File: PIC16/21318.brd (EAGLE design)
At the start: 71.1 x 30.5 mm, 11 parts, among them U2 I50115

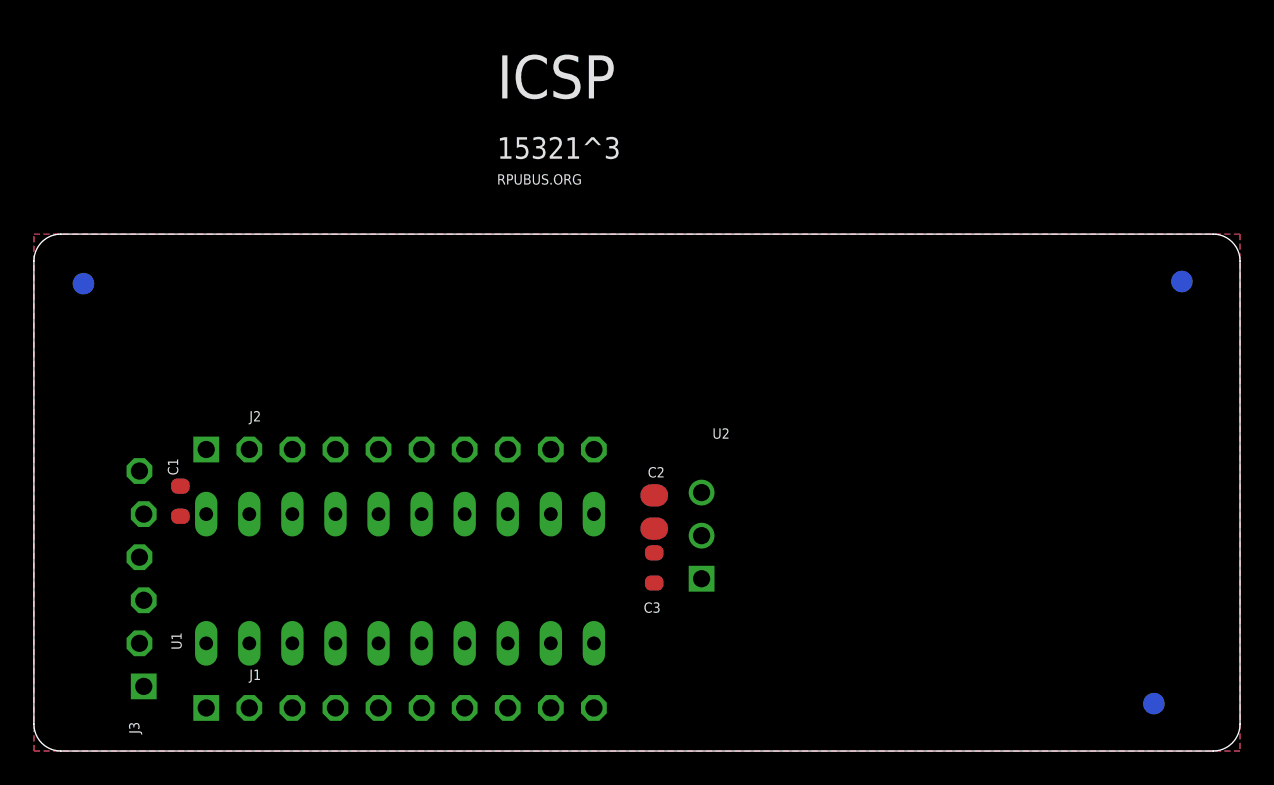
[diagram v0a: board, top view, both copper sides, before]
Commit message: PIC16
8pin, 14pin, and 20pin will work, just keep pin 1 fixed.
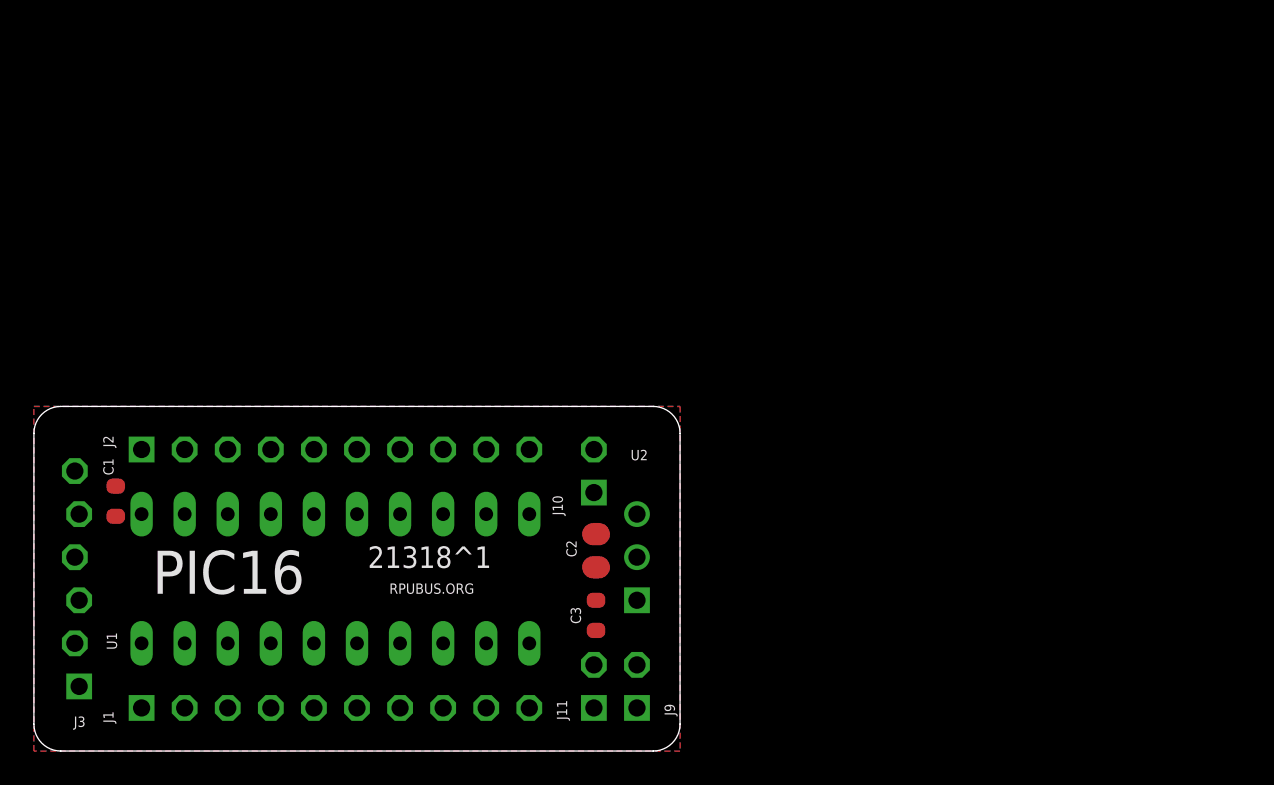
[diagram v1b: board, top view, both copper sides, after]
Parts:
- removed U$2, U$3, U$4: FIDUCIAL1.27, H-Fiducial:FIDUCIAL-1.27
- added J10, J11, J9: (no value), J-HDR2.54mm:1X2
- moved C3 4.42 mm to (33.1, 8.00), turned to 270 degrees
- moved C2 4.12 mm to (33.1, 11.8)
- moved U2 4.02 mm to (35.6, 8.89)
- moved J1 3.81 mm to (6.35, 2.54)
- moved J2 3.81 mm to (6.35, 17.8)
- moved C1 3.81 mm to (4.83, 14.7)
- moved J3 3.81 mm to (2.54, 3.81)
- moved U1 3.81 mm to (17.8, 10.2)
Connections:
- removed net N$1: J3.1, U1.4
- new net RA2: J2.4, U1.17
- new net RA3: J1.4, J3.1, U1.4
- new net RA4: J1.3, U1.3
- new net RA5: J1.2, U1.2
- new net RB4: J2.8, U1.13
- new net RB5: J2.9, U1.12
- new net RB6: J2.10, U1.11
- new net RB7: J1.10, U1.10
- new net RC0: J2.5, U1.16
- new net RC1: J2.6, U1.15
- new net RC2: J2.7, U1.14
- new net RC3: J1.7, U1.7
- new net RC4: J1.6, U1.6
- new net RC5: J1.5, U1.5
- new net RC6: J1.8, U1.8
- new net RC7: J1.9, U1.9
- net 0V: now also J10.1, J10.2, J11.1, J11.2
- net V+: now also J9.1, J9.2
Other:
- board size 71.1 x 30.5 mm -> 38.1 x 20.3 mm
- board text added: "21318^1"
- board text added: "PIC16"
- board text removed: "15321^3"
- board text removed: "ICSP"

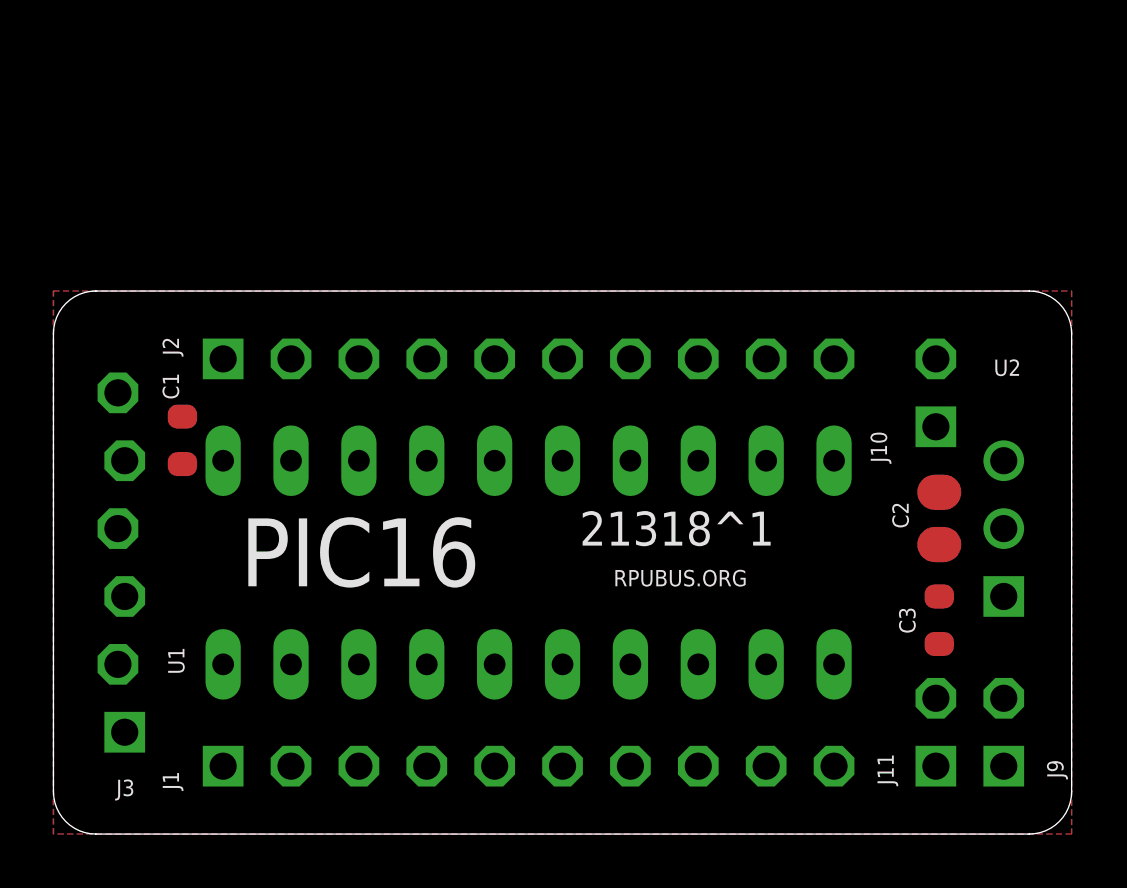
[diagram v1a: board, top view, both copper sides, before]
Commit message: PIC16: add three switches
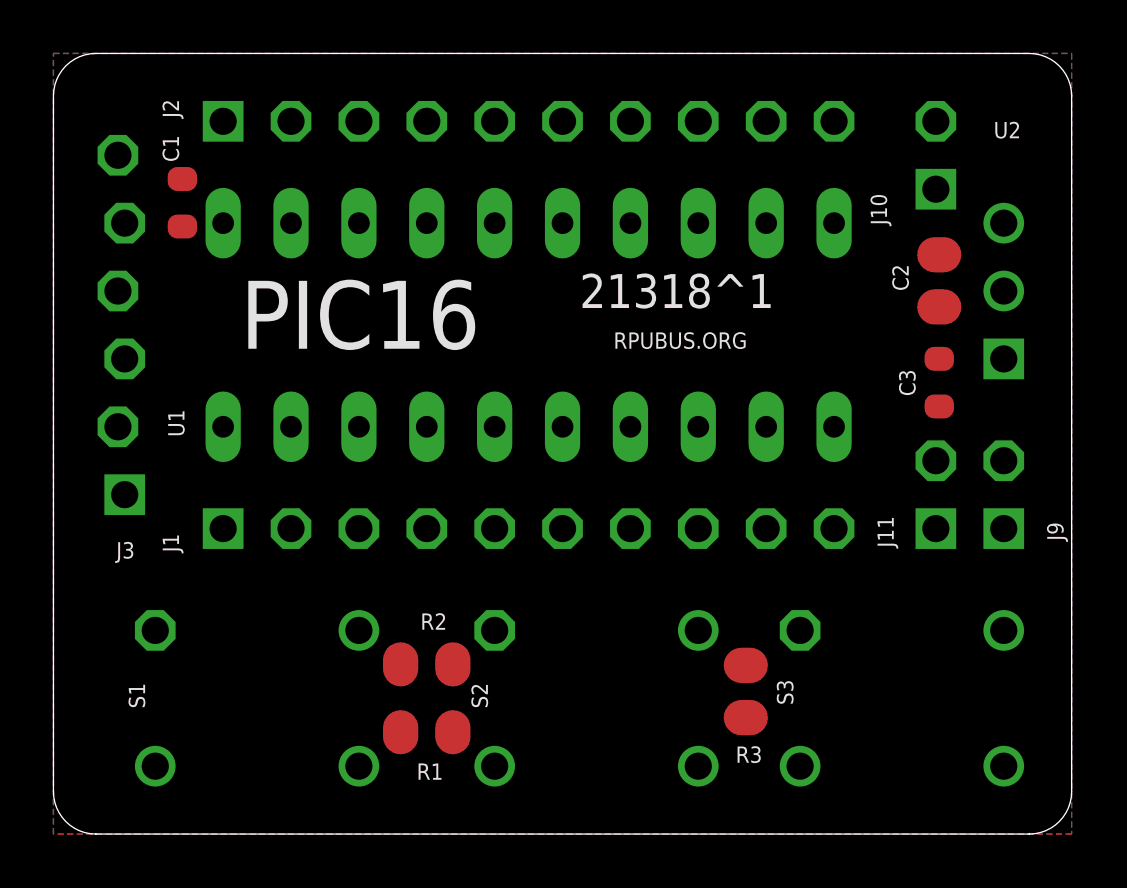
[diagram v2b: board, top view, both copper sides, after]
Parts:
- added R1, R2, R3: 1.82k, R-C:C0805(2012)
- added S1, S2, S3: KSA0M311, S-Tactile:0M311
- moved C1 8.89 mm to (4.83, 23.6)
- moved C2 8.89 mm to (33.1, 20.7)
- moved J1 8.89 mm to (6.35, 11.4)
- moved J11 8.89 mm to (33.0, 11.4)
- moved J2 8.89 mm to (6.35, 26.7)
- moved J9 8.89 mm to (35.6, 11.4)
- moved U1 8.89 mm to (17.8, 19.1)
- moved U2 8.89 mm to (35.6, 17.8)
- moved C3 8.89 mm to (33.1, 16.9)
- moved J10 8.89 mm to (33.0, 24.1)
- moved J3 8.89 mm to (2.54, 12.7)
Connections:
- new net N$1: R2.1, S2.1, S2.2
- new net N$2: R3.1, S3.1, S3.2
- new net N$93: R1.1, S1.1, S1.2
- net 0V: now also S1.3, S1.4, S2.3, S2.4, S3.3, S3.4
- net RC3: now also R1.2
- net RC4: now also R2.2
- net RC5: now also R3.2
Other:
- board size 38.1 x 20.3 mm -> 38.1 x 29.2 mm

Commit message: Buck: looking at the inductor
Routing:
- net +5V: track 0.00 -> 48.0 mm, vias 0 -> 1
- net RC5: track 0.00 -> 19.1 mm, vias 0 -> 2
- net RA3: track 0.00 -> 18.3 mm
- net RC3: track 0.00 -> 17.4 mm, vias 0 -> 2
- net RA1: track 0.00 -> 15.2 mm
- net RC4: track 0.00 -> 14.1 mm, vias 0 -> 2
- net RA0: track 0.00 -> 13.5 mm
- net N$93: track 0.00 -> 12.2 mm, vias 0 -> 1
- net N$2: track 0.00 -> 10.2 mm
- net N$1: track 0.00 -> 9.71 mm
- net V+: track 0.00 -> 8.76 mm
- net RC2: track 0.00 -> 3.81 mm
- net RC1: track 0.00 -> 3.81 mm
- net RC0: track 0.00 -> 3.81 mm
- net RB6: track 0.00 -> 3.81 mm
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
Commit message: PIC16: schematic
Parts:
- C1: value (none) -> .1uF
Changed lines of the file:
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@@
 <attribute name="NAME" x="3.048" y="10.922" size="0.6096" layer="25" ratio="10" rot="R180"/>
 </element>
-<element name="C1" library="C-C" package="C0603(1608)" value="" x="4.826" y="23.622" smashed="yes" rot="R90">
+<element name="C1" library="C-C" package="C0603(1608)" value=".1uF" x="4.826" y="23.622" smashed="yes" rot="R90">
 <attribute name="NAME" x="4.699" y="25.146" size="0.6096" layer="25" rot="R90"/>
 <attribute name="VALUE" x="5.08" y="22.987" size="0.4064" layer="27" rot="R90"/>
